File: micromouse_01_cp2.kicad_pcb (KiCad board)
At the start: 4 copper layers, 51.9 x 53 mm, 98 parts, among them IC1 ESP32-S3FH4R2, IC2 MPU-6500, IC3 AS5047P-ATSM, IC4 AS5047P-ATSM, IC5 DRV8835DSSR, IC6 PCA9632TK,118, J1 Conn_01x02, J2 USB_B_Micro, M1 MK06-4.5, M2 MK06-4.5, M3 Fan_Motor, Q1 MCM3400A-TP, Q2 MCM3400A-TP, Q3 MCM3400A-TP, Q4 SSM6J808R_LXHF, SW1 SSSS810701, SW2 SW_Push, U1 SMT-0440-S-R, U2 LBR-127HLD, U3 LBR-127HLD, U4 LBR-127HLD, U5 LBR-127HLD, U6 LXDC55FAAA-203, U7 RTV-104DF333-S-40.000-TR

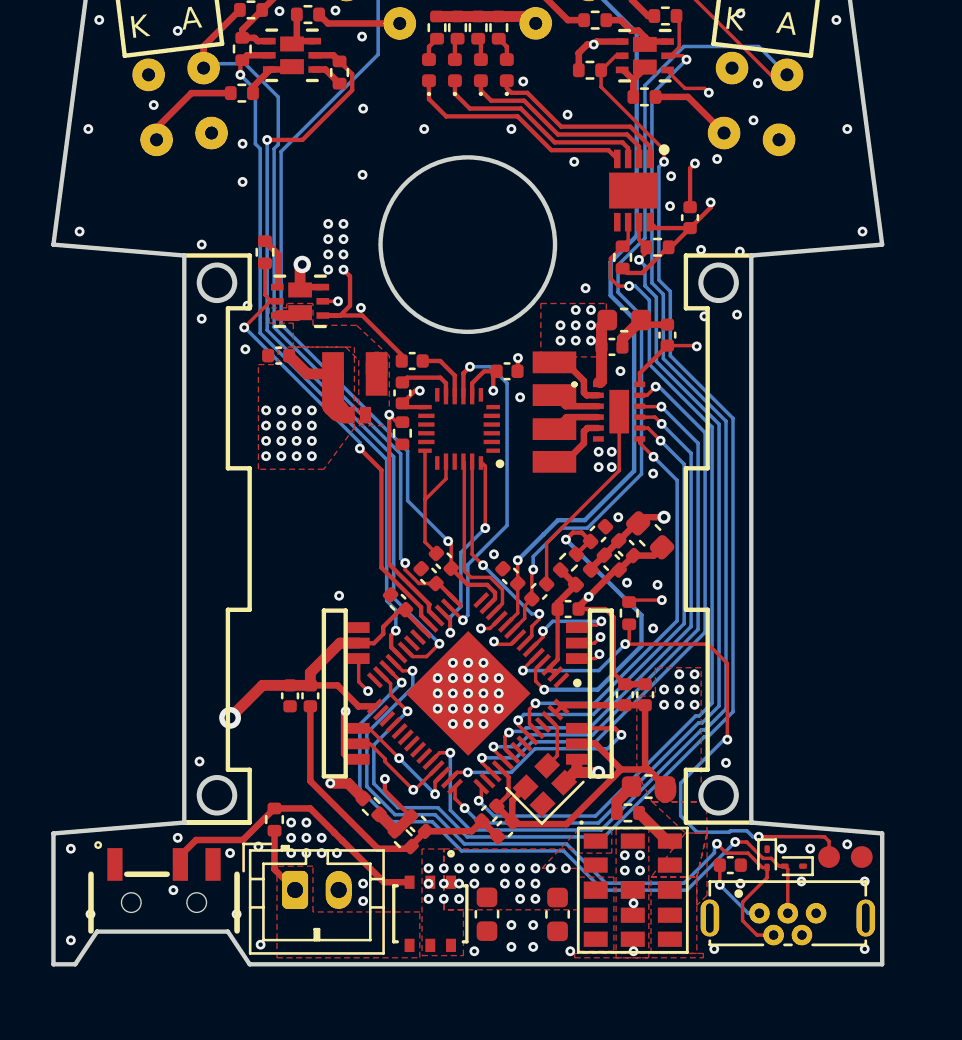
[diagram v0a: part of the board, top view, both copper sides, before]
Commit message: [add]LED追加
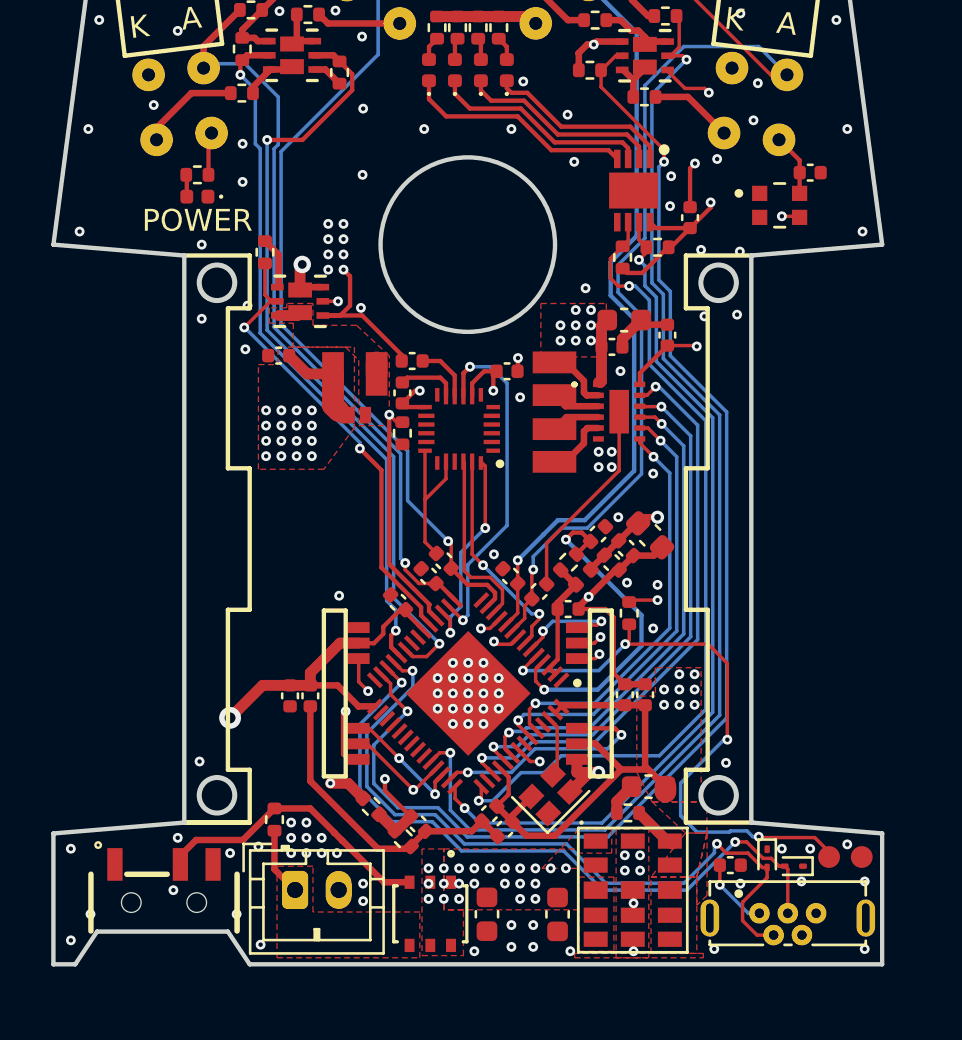
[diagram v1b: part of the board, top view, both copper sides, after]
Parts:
- added C8: 0.1u, Capacitor_SMD:C_0402_1005Metric, F.Cu at (166.7, 73.7)
- added D6: POWER, LED_SMD:LED_0402_1005Metric, F.Cu at (138.6, 74.8)
- added R16: 1k, Resistor_SMD:R_0402_1005Metric, F.Cu at (138.6, 73.8)
- added U8: WS2812-2020, footprints:LED_WS2812-2020, F.Cu at (165.3, 75.2)
- moved U7 0.50 mm to (154.8, 102.2)
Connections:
- IC1 pad 49: unconnected-(IC1-U0TXD-Pad49) -> NeoPixel
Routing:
- net NeoPixel: track 0.00 -> 33.4 mm, vias 0 -> 2
- net Net-(D6-A): track 0.00 -> 1.01 mm
- net LED_SCL: track 38.6 -> 37.8 mm
- net +3V3: track 264.1 -> 264.7 mm

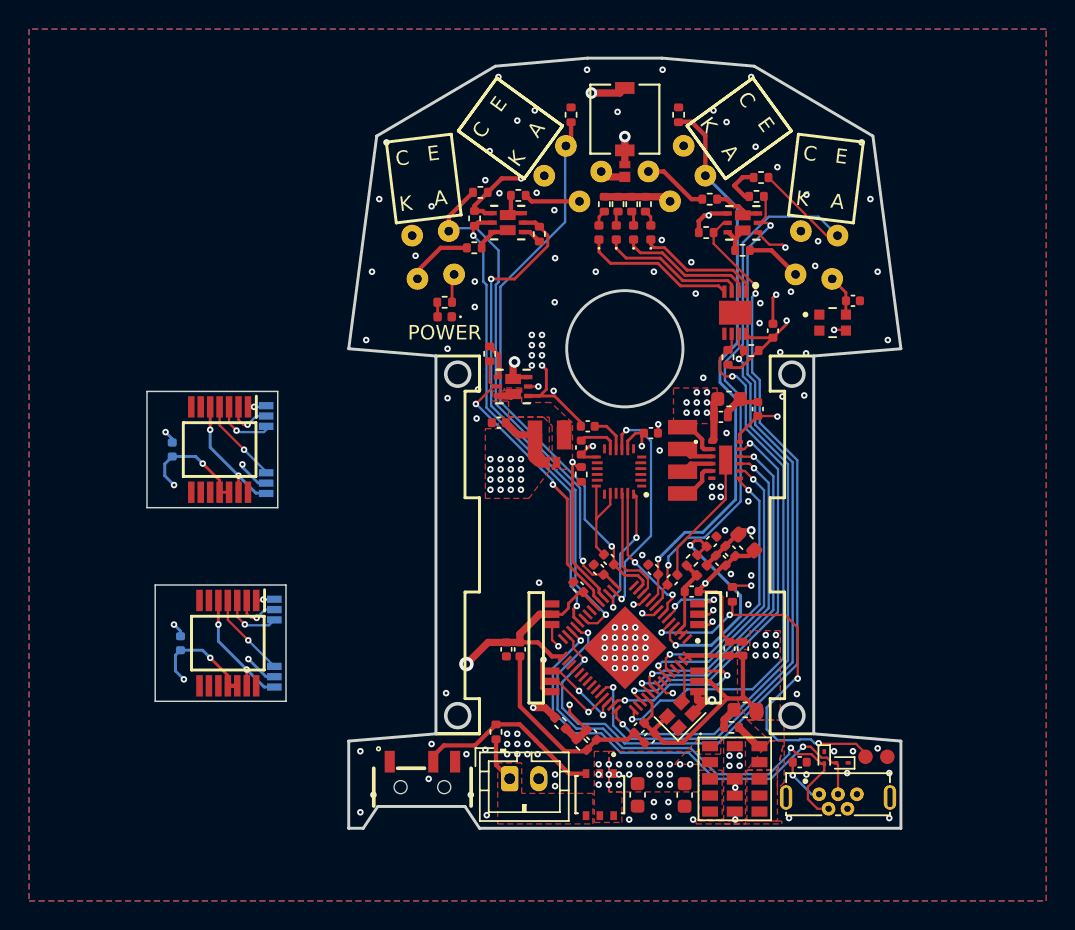
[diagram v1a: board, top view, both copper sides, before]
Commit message: エンコーダ基板ビア打ち エラー修正
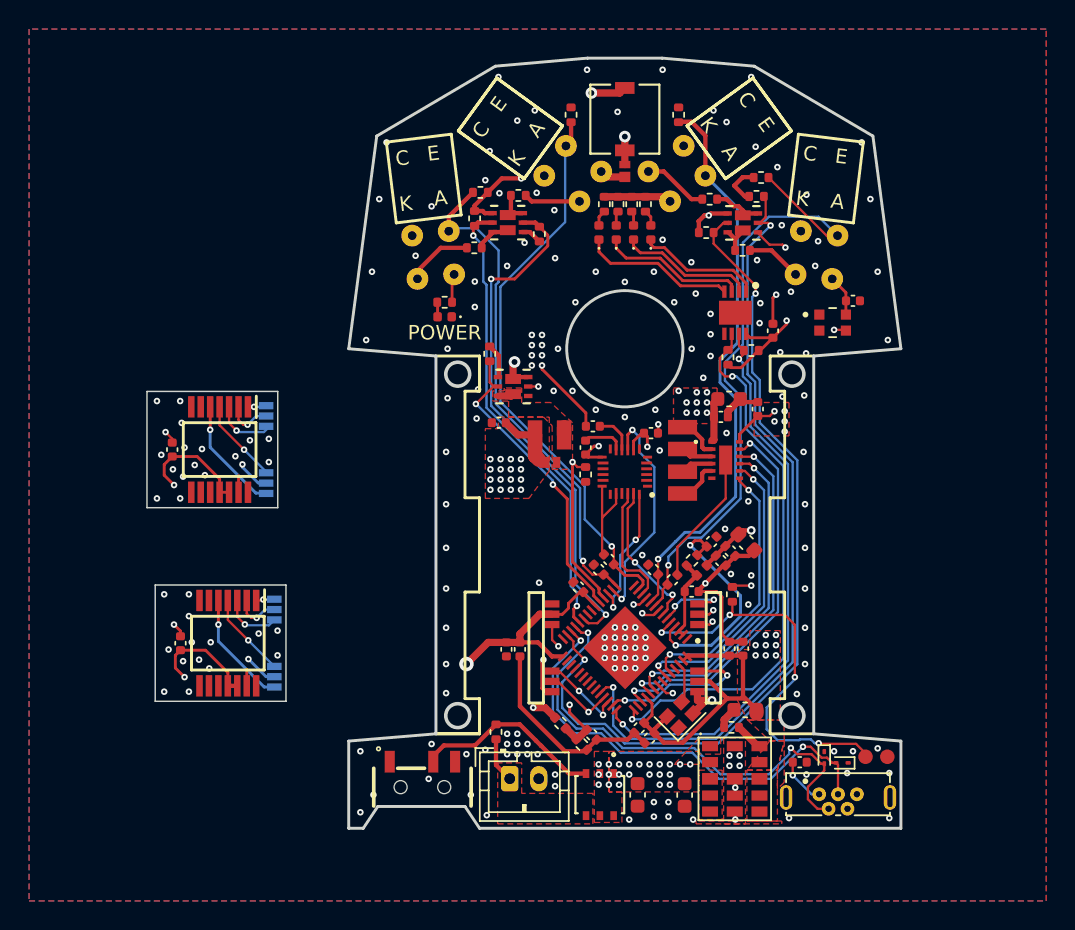
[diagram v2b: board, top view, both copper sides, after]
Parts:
- C6, C7: moved to F.Cu
- moved IC2 0.40 mm to (151.0, 85.5)
- moved C4 0.35 mm to (148.8, 82.3)
- moved C3 0.30 mm to (148.3, 83.8)
- moved R22 0.30 mm to (148.3, 85.7)
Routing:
- net GND: track 101.6 -> 98.9 mm, vias 148 -> 200
- net IMU_MISO: track 16.1 -> 15.6 mm
- net +3V3: track 264.7 -> 264.3 mm, vias 22 -> 24

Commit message: [fix]アンテナ除去
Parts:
- moved R17 1.35 mm to (141.7, 76.0)
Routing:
- net GND: track 98.9 -> 102.1 mm, vias 200 -> 225
- net USB_D-: track 33.4 -> 32.2 mm
- net USB_D+: track 31.6 -> 30.8 mm
- net BUZZER: track 21.5 -> 22.2 mm
- net IMU_MISO: track 15.6 -> 15.0 mm

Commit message: commit
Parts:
- moved C35 0.85 mm to (153.5, 103.5), turned to 135 degrees
- moved R13 0.19 mm to (156.8, 66.9)
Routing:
- net +3V3: track 264.3 -> 265.3 mm
- net GND: track 102.1 -> 103.0 mm, vias 225 -> 226

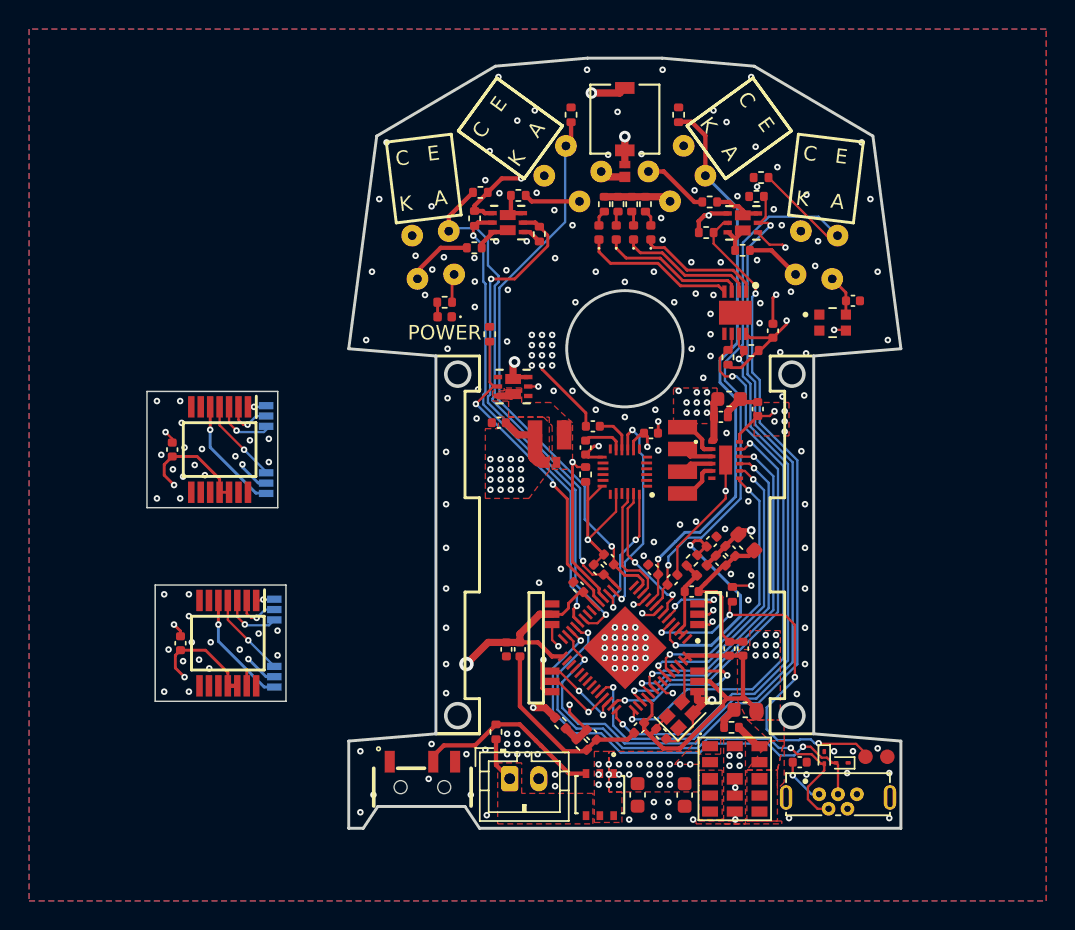
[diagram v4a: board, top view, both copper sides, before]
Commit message: エンコーダ基板修正 LBR-127HLDスルーホール修正
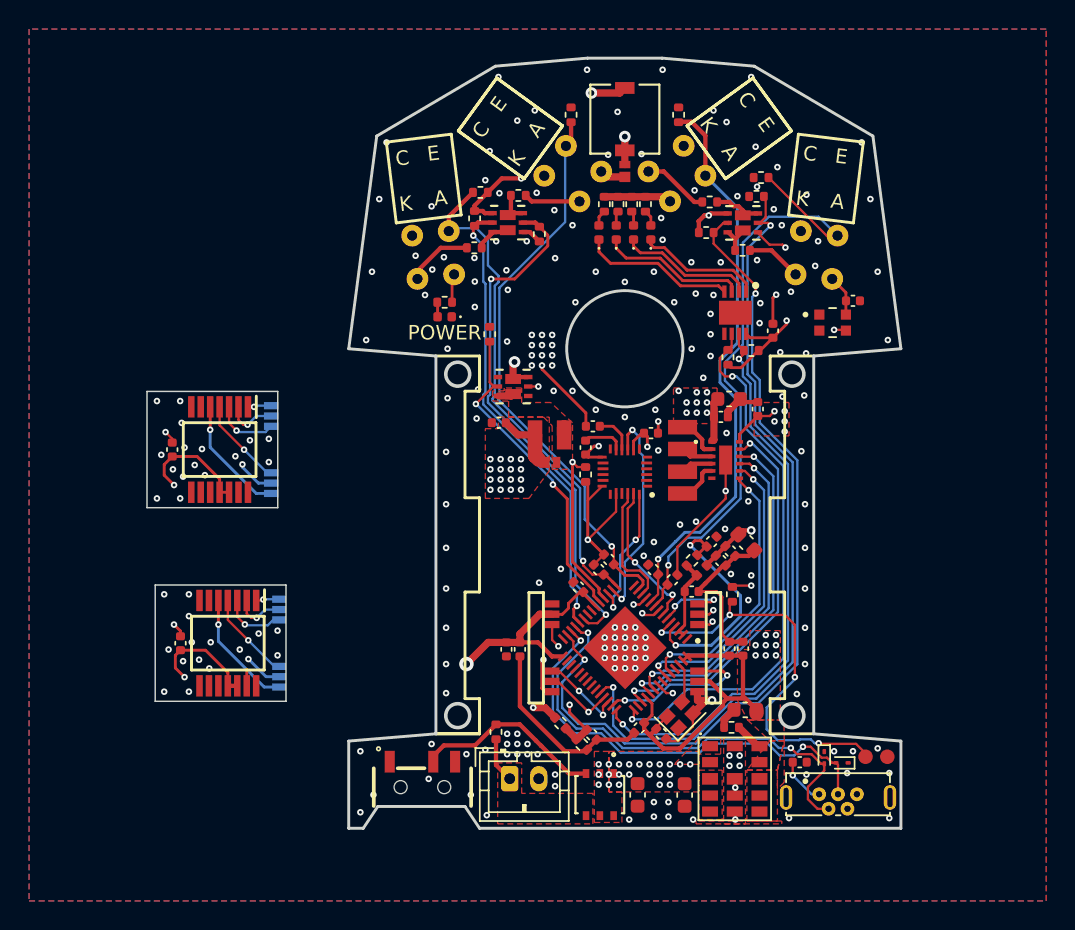
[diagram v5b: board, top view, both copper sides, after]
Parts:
- moved REF** 0.35 mm to (126.7, 83.9)
- moved REF** 0.35 mm to (127.2, 97.3)
